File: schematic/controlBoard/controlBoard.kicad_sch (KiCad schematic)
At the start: 40 parts, among them CON0 PINHD-1X10, IC2 DS3231/SO, IC3 LM1117?-MP, IC4 ESP12ESMD, T1 BC547, T2 BC547, Y1 12MHz

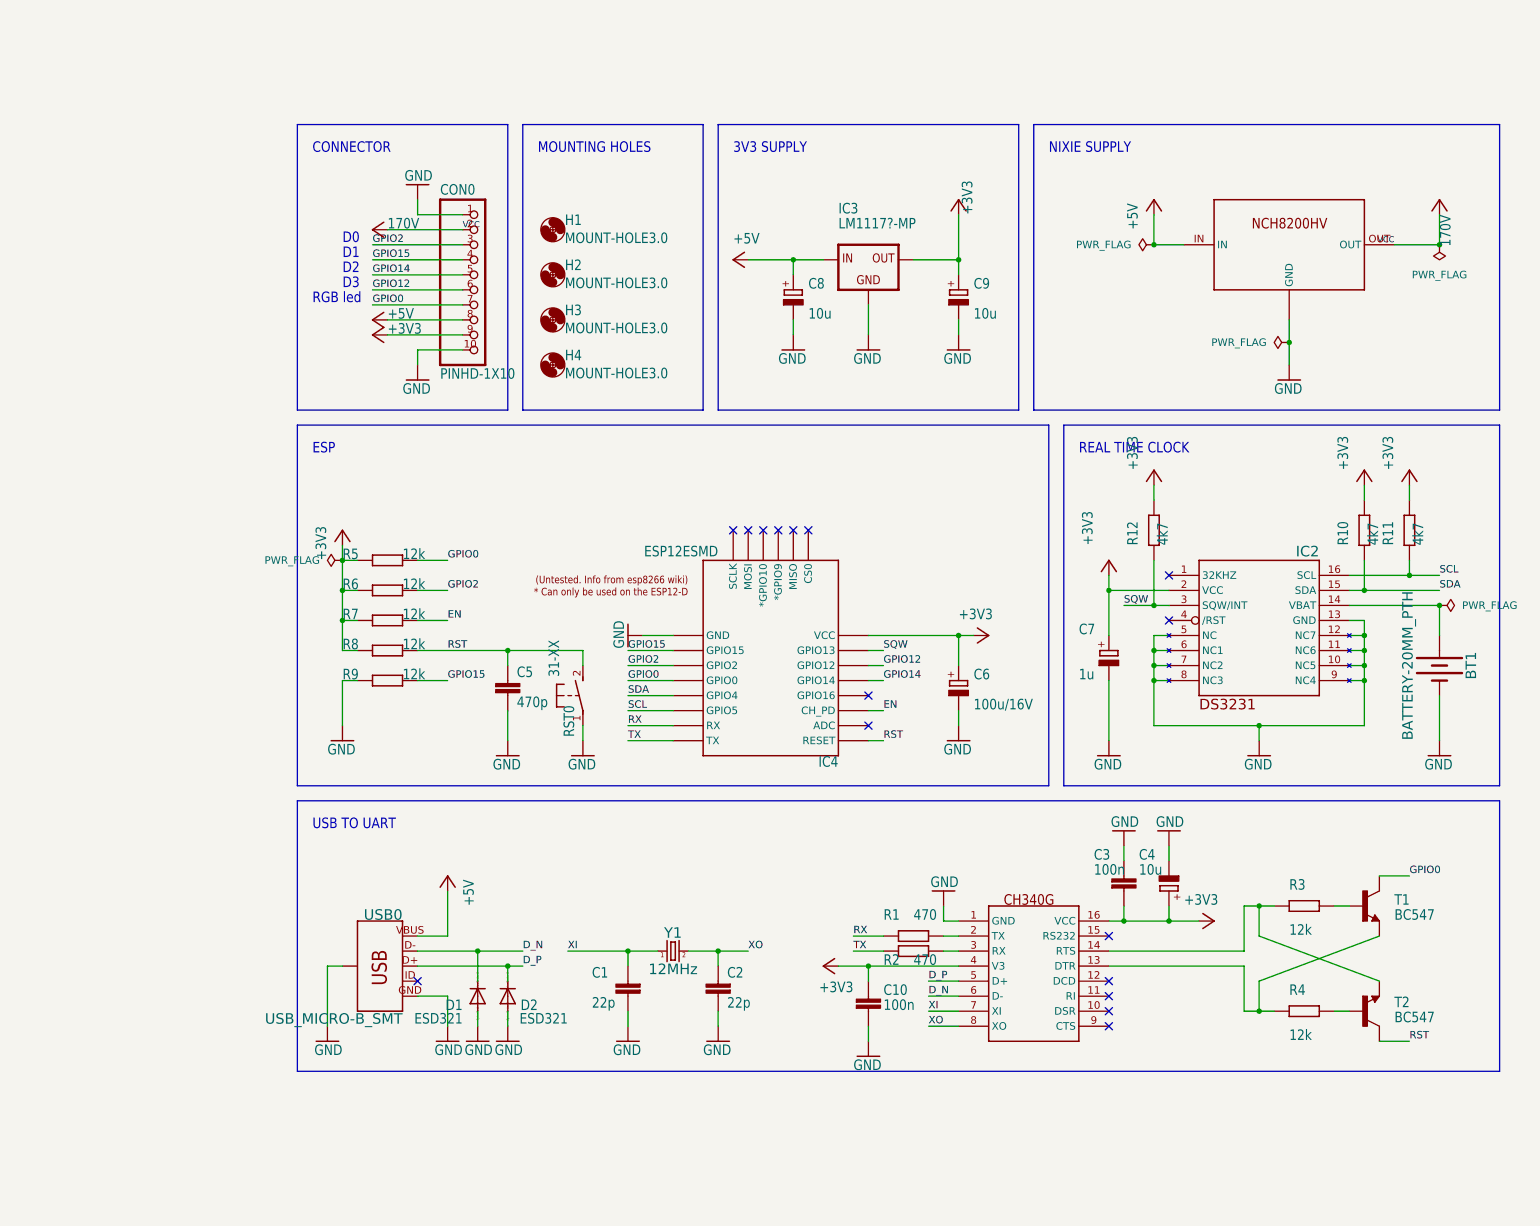
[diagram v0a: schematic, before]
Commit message: Use usb type C connector and re-wire control board with KiCad components
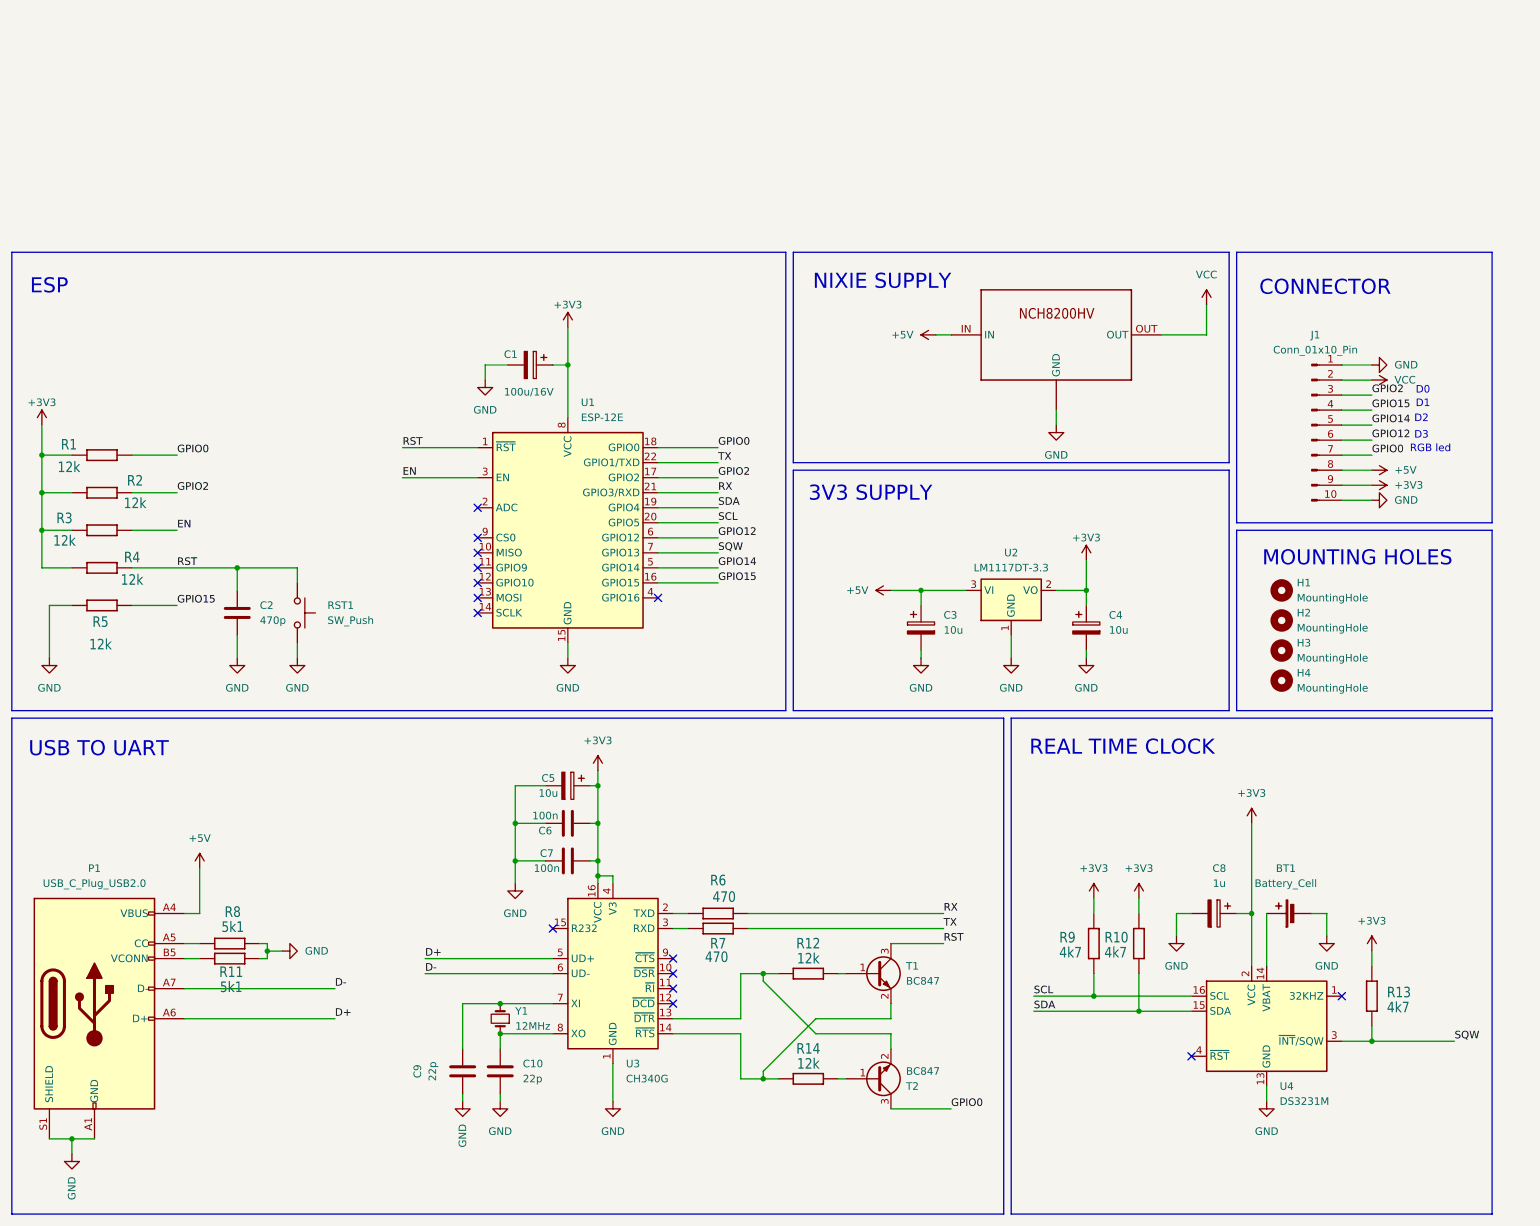
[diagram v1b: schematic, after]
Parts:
- removed BT1: BATTERY-20MM_PTH, controlBoard:BATTCOM_20MM_PTH, symbol controlBoard-eagle-import:BATTERY-20MM_PTH
- removed C1, C2: 22p, controlBoard:C0603, symbol controlBoard-eagle-import:C-EUC0603
- removed C10, C3: 100n, controlBoard:C0603, symbol controlBoard-eagle-import:C-EUC0603
- removed C4, C8, C9: 10u, controlBoard:SMC_A, symbol controlBoard-eagle-import:CPOL-EUSMCA
- removed C5: 470p, controlBoard:C0603, symbol controlBoard-eagle-import:C-EUC0603
- removed C6: 100u/16V, controlBoard:SMC_D, symbol controlBoard-eagle-import:CPOL-EUSMCD
- removed C7: 1u, controlBoard:SMC_A, symbol controlBoard-eagle-import:CPOL-EUSMCA
- removed CON0: PINHD-1X10, controlBoard:1X10, symbol controlBoard-eagle-import:PINHD-1X10
- removed D1, D2: ESD321, controlBoard:SOD523, symbol controlBoard-eagle-import:DIODE-SOD523
- removed H1, H2, H3, H4: MOUNT-HOLE3.0, controlBoard:3,0, symbol controlBoard-eagle-import:MOUNT-HOLE3.0
- removed IC2: DS3231/SO, controlBoard:SO16W, symbol controlBoard-eagle-import:DS3231/SO
- removed IC3: LM1117?-MP, controlBoard:SOT223, symbol controlBoard-eagle-import:LM1117?-MP
- removed IC4: ESP12ESMD, controlBoard:ESP12E-SMD, symbol controlBoard-eagle-import:ESP12ESMD
- removed RST0: 31-XX, controlBoard:B3F-31XX, symbol controlBoard-eagle-import:31-XX
- removed T1, T2: BC547, controlBoard:SOT23-BEC, symbol controlBoard-eagle-import:-NPN-SOT23-BEC
- removed U$2: CH340G, controlBoard:SOIC16, symbol controlBoard-eagle-import:CH340G
- removed USB0: USB_MICRO-B_SMT, controlBoard:USB-MICROB, symbol controlBoard-eagle-import:USB_MICRO-B_SMT
- removed Y1: 12MHz, controlBoard:CRYSTAL-SMD-5X3.2-4PAD, symbol controlBoard-eagle-import:CRYSTAL-12MHZ{dblquote}
- added BT1: Battery_Cell, Battery:BatteryHolder_MYOUNG_BS-07-A1BJ001_CR2032, symbol Device:Battery_Cell
- added C1: 100u/16V, Capacitor_Tantalum_SMD:CP_EIA-7343-31_Kemet-D, symbol Device:C_Polarized
- added C10, C9: 22p, Capacitor_SMD:C_0603_1608Metric, symbol Device:C
- added C2: 470p, Capacitor_SMD:C_0603_1608Metric, symbol Device:C
- added C3, C4, C5: 10u, Capacitor_Tantalum_SMD:CP_EIA-3216-10_Kemet-I, symbol Device:C_Polarized
- added C6, C7: 100n, Capacitor_SMD:C_0603_1608Metric, symbol Device:C
- added C8: 1u, Capacitor_Tantalum_SMD:CP_EIA-3216-10_Kemet-I, symbol Device:C_Polarized
- added H1, H2, H3, H4: MountingHole, MountingHole:MountingHole_3.2mm_M3, symbol Mechanical:MountingHole
- added J1: Conn_01x10_Pin, Connector_PinHeader_2.54mm:PinHeader_1x10_P2.54mm_Vertical, symbol Connector:Conn_01x10_Pin
- added P1: USB_C_Plug_USB2.0, Connector_USB:USB_C_Receptacle_GCT_USB4105-xx-A_16P_TopMnt_Horizontal, symbol Connector:USB_C_Plug_USB2.0
- added R13: 4k7, Resistor_SMD:R_0603_1608Metric, symbol controlBoard-eagle-import:R-EU_R0603
- added R14: 12k, Resistor_SMD:R_0603_1608Metric, symbol controlBoard-eagle-import:R-EU_R0603
- added RST1: SW_Push, Button_Switch_THT:SW_Tactile_SPST_Angled_PTS645Vx31-2LFS, symbol Switch:SW_Push
- added T1, T2: BC847, Package_TO_SOT_SMD:SOT-23, symbol Transistor_BJT:BC847
- added U1: ESP-12E, RF_Module:ESP-12E, symbol RF_Module:ESP-12E
- added U2: LM1117DT-3.3, Package_TO_SOT_SMD:TO-252-3_TabPin2, symbol Regulator_Linear:LM1117DT-3.3
- added U3: CH340G, Package_SO:SOIC-16_3.9x9.9mm_P1.27mm, symbol Interface_USB:CH340G
- added U4: DS3231M, Package_SO:SOIC-16W_7.5x10.3mm_P1.27mm, symbol Timer_RTC:DS3231M
- added Y1: 12MHz, controlBoard:CRYSTAL-SMD-5X3.2-4PAD, symbol Device:Crystal_Small
- R1, R2: value 470 -> 12k; footprint controlBoard:R0603 -> Resistor_SMD:R_0603_1608Metric
- R10, R3, R4, R5: footprint controlBoard:R0603 -> Resistor_SMD:R_0603_1608Metric
- R11: value 4k7 -> 5k1; footprint controlBoard:R0603 -> Resistor_SMD:R_0603_1608Metric
- R12: value 4k7 -> 12k; footprint controlBoard:R0603 -> Resistor_SMD:R_0603_1608Metric
- R6, R7: value 12k -> 470; footprint controlBoard:R0603 -> Resistor_SMD:R_0603_1608Metric
- R8: value 12k -> 5k1; footprint controlBoard:R0603 -> Resistor_SMD:R_0603_1608Metric
- R9: value 12k -> 4k7; footprint controlBoard:R0603 -> Resistor_SMD:R_0603_1608Metric
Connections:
- net +3V3: now also R1.2, R10.2, R2.2, R3.2, R4.2, R9.2, C1.1, C4.1, C5.1, C6.1, C7.2, C8.1, J1.9 (Pin_9), R13.2, U1.8 (VCC), U2.2 (VO), U3.16 (VCC), U3.4 (V3), U4.2 (VCC); no longer R10.1, R11.1, R12.1, R5.2, R6.2, R7.2, R8.2
- net +5V: now also C3.1, J1.8 (Pin_8), P1.A4 (VBUS), P1.A9 (VBUS), P1.B4 (VBUS), P1.B9 (VBUS), U2.3 (VI)
- net EN: now also R3.1, U1.3 (EN); no longer R7.1
- net GND: now also R11.2, R5.2, R8.2, BT1.2 (-), C1.2, C10.2, C2.2, C3.2, C4.2, C5.2, C6.2, C7.1, C8.2, C9.2, J1.1 (Pin_1), J1.10 (Pin_10), P1.A1 (GND), P1.A12 (GND), P1.B1 (GND), P1.B12 (GND), P1.S1 (SHIELD), RST1.2, U1.15 (GND), U2.1 (GND), U3.1 (GND), U4.10 (GND), U4.11 (GND), U4.12 (GND), U4.13 (GND), U4.5 (GND), U4.6 (GND), U4.7 (GND), U4.8 (GND), U4.9 (GND); no longer R9.2
- net GPIO0: now also R1.1, J1.7 (Pin_7), T2.3 (C), U1.18 (GPIO0); no longer R5.1
- net GPIO12: now also J1.6 (Pin_6), U1.6 (GPIO12)
- net GPIO14: now also J1.5 (Pin_5), U1.5 (GPIO14)
- net GPIO15: now also R5.1, J1.4 (Pin_4), U1.16 (GPIO15); no longer R9.1
- net GPIO2: now also R2.1, J1.3 (Pin_3), U1.17 (GPIO2); no longer R6.1
- net RST: now also R4.1, C2.1, RST1.1, T1.3 (C), U1.1 (~{RST}); no longer R8.1
- net RX: now also R6.2, U1.21 (GPIO3/RXD); no longer R1.2
- net SCL: now also R9.1, U1.20 (GPIO5), U4.16 (SCL); no longer R11.2
- net SDA: now also R10.1, U1.19 (GPIO4), U4.15 (SDA); no longer R10.2
- net SQW: now also R13.1, U1.7 (GPIO13), U4.3 (~{INT}/SQW); no longer R12.2
- net TX: now also R7.2, U1.22 (GPIO1/TXD); no longer R2.2
- net 170V renamed VCC
- net VCC: now also J1.2 (Pin_2)
- new net: R12.2, T1.1 (B)
- new net: R14.1, T1.2 (E), U3.14 (~{RTS})
- new net: P1.A5 (CC), R8.1
- new net: P1.B5 (VCONN), R11.1
- new net: C9.1, U3.7 (XI), Y1.2
- new net: R12.1, T2.2 (E), U3.13 (~{DTR})
- new net: C10.1, U3.8 (XO), Y1.1
- new net: R14.2, T2.1 (B)
- new net: BT1.1 (+), U4.14 (VBAT)
- new net: R6.1, U3.2 (TXD)
- new net: R7.1, U3.3 (RXD)
- new net D+: P1.A6 (D+), U3.5 (UD+)
- new net D-: P1.A7 (D-), U3.6 (UD-)
- no-connect marks 16 -> 15

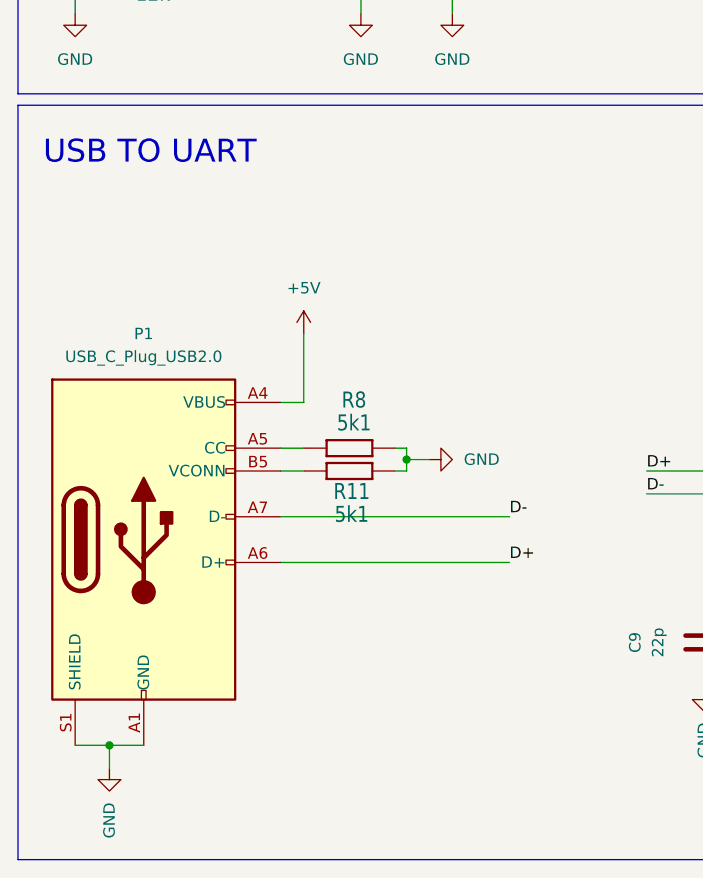
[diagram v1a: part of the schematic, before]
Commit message: Update control board with updated usb-c wiring
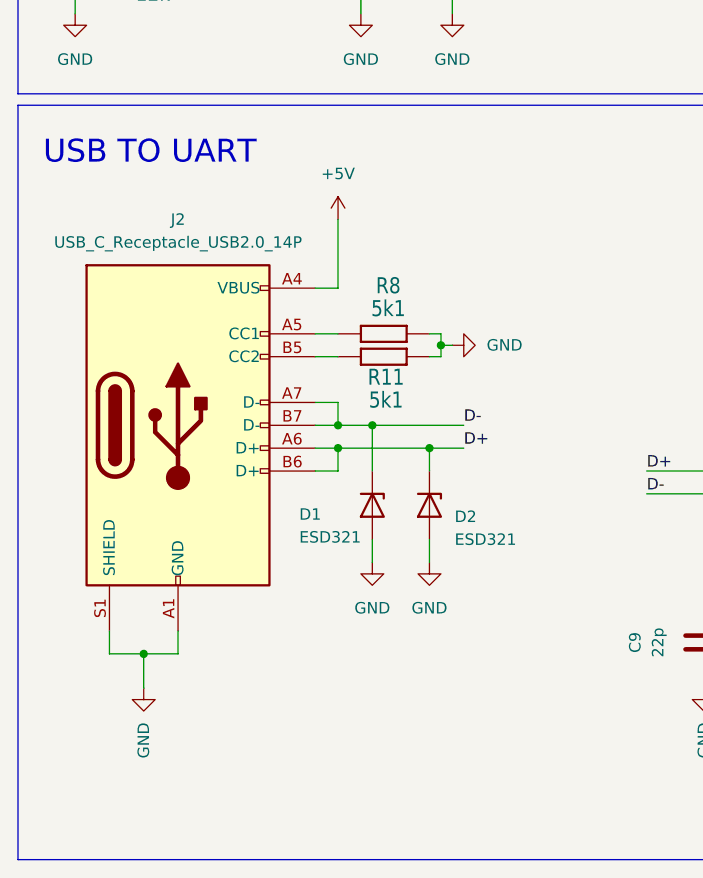
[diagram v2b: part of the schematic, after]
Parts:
- removed P1: USB_C_Plug_USB2.0, Connector_USB:USB_C_Receptacle_GCT_USB4105-xx-A_16P_TopMnt_Horizontal, symbol Connector:USB_C_Plug_USB2.0
- added D1, D2: ESD321, Diode_SMD:D_SOD-523, symbol Device:D_Zener
- added J2: USB_C_Receptacle_USB2.0_14P, Connector_USB:USB_C_Receptacle_GCT_USB4105-xx-A_16P_TopMnt_Horizontal, symbol Connector:USB_C_Receptacle_USB2.0_14P
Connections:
- net +5V: now also J2.A4 (VBUS), J2.A9 (VBUS), J2.B4 (VBUS), J2.B9 (VBUS)
- net D+: now also D2.1 (K), J2.A6 (D+), J2.B6 (D+)
- net D-: now also D1.1 (K), J2.A7 (D-), J2.B7 (D-)
- net GND: now also D1.2 (A), D2.2 (A), J2.A1 (GND), J2.A12 (GND), J2.B1 (GND), J2.B12 (GND), J2.S1 (SHIELD)
- net at R8.1: now also J2.A5 (CC1)
- net at R11.1: now also J2.B5 (CC2)
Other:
- moved on the sheet: R11, R8
